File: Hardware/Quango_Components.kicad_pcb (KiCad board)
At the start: 2 copper layers, 80.7 x 100 mm, 156 parts, among them J1 Conn_01x12_Male, J2 Conn_01x12_Male, J3 Conn_01x12_Male, J4 Conn_01x12_Male, J5 SWD_Header, J6 Eurorack_10_pin_power, Q1 MMBT3904, U1 LM1117-3.3, U10 TL074, U11 TL074, U12 TL074, U13 TL074, U14 TL074, U2 STM32G473V, U3 LM1117-5.0, U4 PS508, U5 MCP6002, U6 AS3364, U7 AS3364, U8 AD5676, U9 MCP48CMB21, Y1 8MHz 20pF

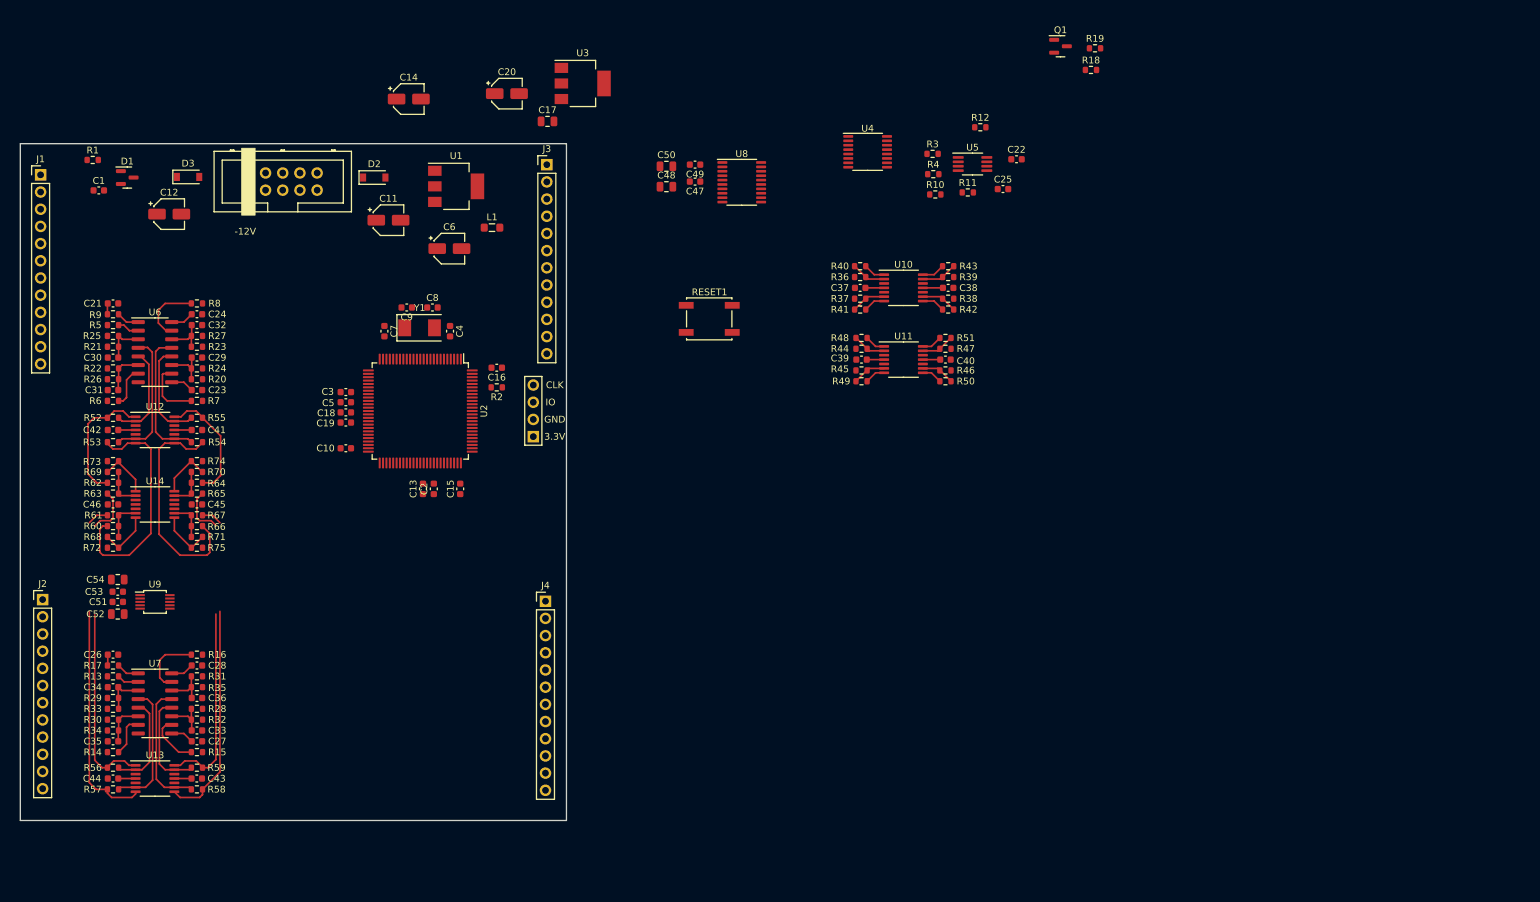
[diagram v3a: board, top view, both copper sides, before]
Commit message: Main components positioned
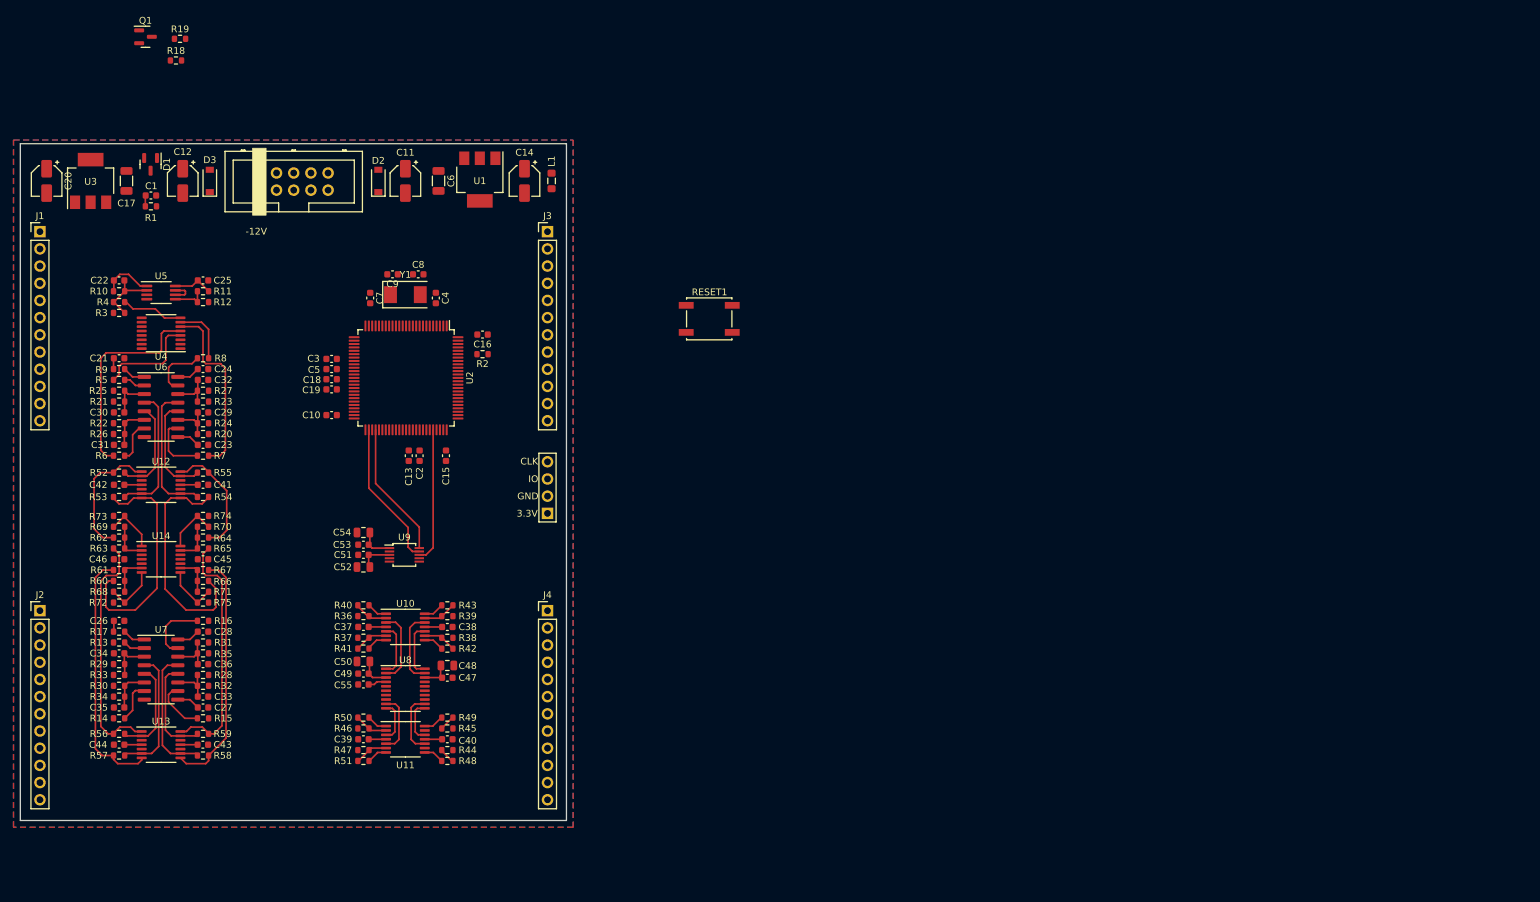
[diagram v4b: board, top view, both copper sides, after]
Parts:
- added C55: 100nF, Capacitor_SMD:C_0603_1608Metric, F.Cu at (100.8, 118.9)
- C11: value 22uF -> 47uF
- C17: footprint Capacitor_SMD:C_0805_2012Metric -> Capacitor_SMD:C_1206_3216Metric
- C6: value 22uF -> 10uF; footprint Capacitor_SMD:CP_Elec_4x5.8 -> Capacitor_SMD:C_1206_3216Metric
- moved Q1 135.2 mm to (68.6, 23.2)
- moved R18 135.2 mm to (73.1, 26.7)
- moved R19 135.2 mm to (73.7, 23.5)
- moved C22 133.8 mm to (64.7, 59.2)
- moved R3 122.5 mm to (64.7, 64.0), turned to 180 degrees
- moved R4 121.8 mm to (64.7, 62.4)
- moved R10 121.4 mm to (64.7, 60.8)
- moved U5 121.4 mm to (70.9, 61.0)
- moved C25 119.0 mm to (77.1, 59.2)
- moved R12 117.7 mm to (77.1, 62.4), turned to 180 degrees
- moved R11 113.9 mm to (77.1, 60.8)
- moved U4 107.8 mm to (70.9, 67.0), turned to 180 degrees
- moved R51 106.3 mm to (100.8, 130.2), turned to 180 degrees
- moved R47 104.5 mm to (100.8, 128.6), turned to 0 degrees
- moved R46 101.0 mm to (100.8, 125.4), turned to 0 degrees
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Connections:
- U11 pad 1: /CV_OUT_B1 -> /CV_OUT_B3
- U11 pad 10: /DAC_B3 -> /DAC_B1
- U11 pad 12: /DAC_B4 -> /DAC_B2
- U11 pad 13: Net-(R47-Pad2) -> Net-(R45-Pad2)
- U11 pad 14: /CV_OUT_B4 -> /CV_OUT_B2
- U11 pad 2: Net-(R44-Pad2) -> Net-(R46-Pad2)
- U11 pad 3: /DAC_B1 -> /DAC_B3
- U11 pad 5: /DAC_B2 -> /DAC_B4
- U11 pad 6: Net-(R45-Pad2) -> Net-(R47-Pad2)
- U11 pad 7: /CV_OUT_B2 -> /CV_OUT_B4
- U11 pad 8: /CV_OUT_B3 -> /CV_OUT_B1
- U11 pad 9: Net-(R46-Pad2) -> Net-(R44-Pad2)
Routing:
- net /AudioA2_In: track 0.00 -> 30.7 mm
- net /AudioA3_In: track 0.00 -> 26.7 mm
- net /SPI2_SCK: track 0.00 -> 21.6 mm
- net /SPI2_MOSI: track 0.00 -> 20.1 mm
- net /SPI2_MISO: track 0.00 -> 19.9 mm
- net /AudioA1_In: track 0.00 -> 15.2 mm
- net +3.3V: track 0.00 -> 13.8 mm
- net /DAC_A1: track 0.00 -> 11.1 mm
- net /DAC_A4: track 0.00 -> 11.0 mm
- net Net-(C22-Pad2): track 0.00 -> 9.47 mm
- net Net-(R4-Pad2): track 0.00 -> 9.22 mm
- net /DAC_B1: track 0.00 -> 9.10 mm
- net /DAC_B4: track 0.00 -> 9.10 mm
- net +5V: track 0.00 -> 8.97 mm
- net /AudioA4_In: track 0.00 -> 8.87 mm
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- added copper zone on B.Cu, net GND
- added copper zone on F.Cu, net GND

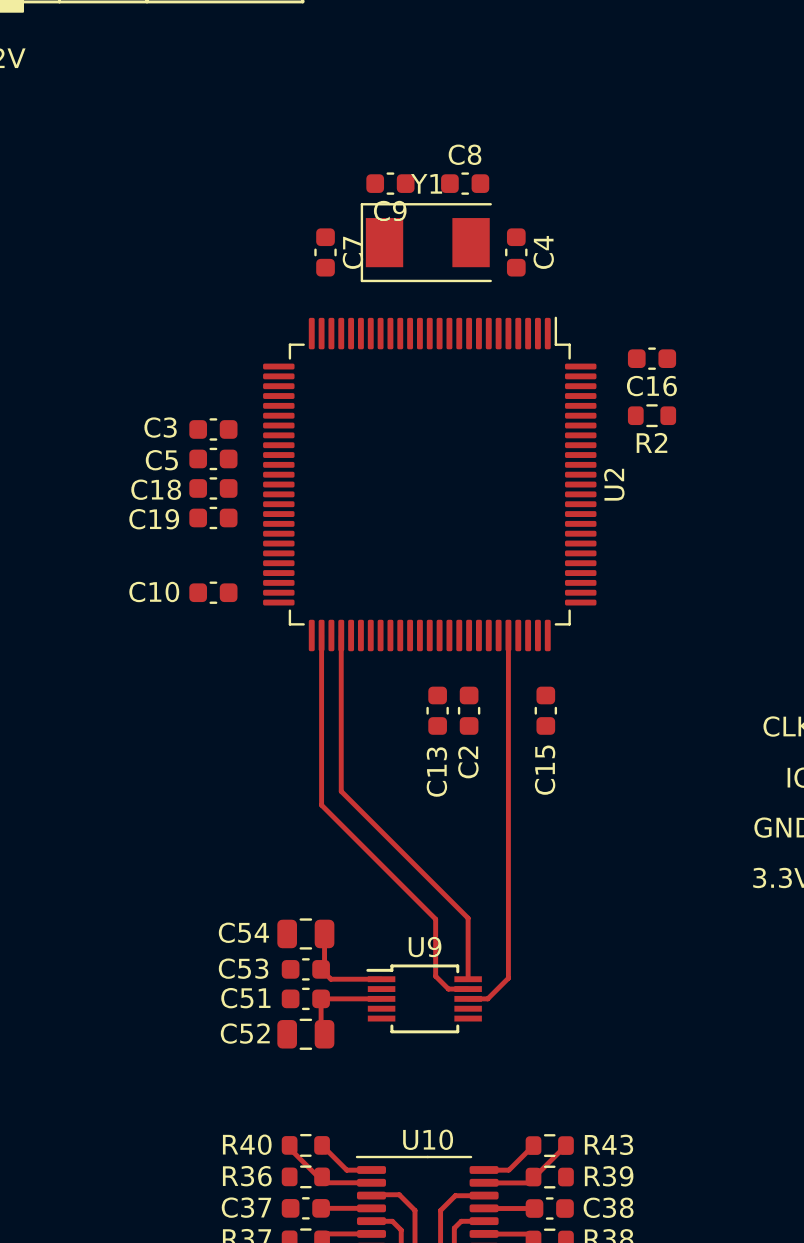
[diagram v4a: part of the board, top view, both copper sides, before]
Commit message: Added LED resistors
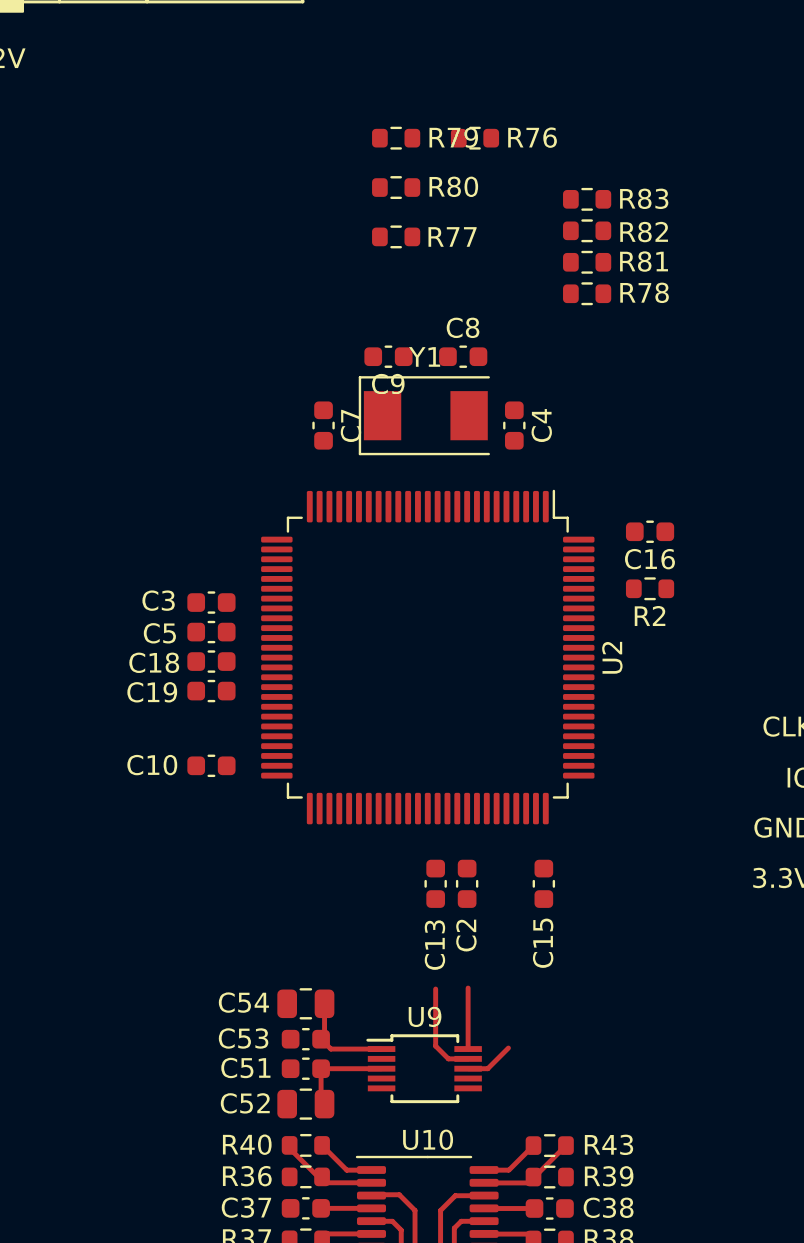
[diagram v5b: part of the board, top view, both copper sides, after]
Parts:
- added R76: 560, Resistor_SMD:R_0603_1608Metric, F.Cu at (109.4, 56.0)
- added R77: 560, Resistor_SMD:R_0603_1608Metric, F.Cu at (105.4, 61.0)
- added R78: 560, Resistor_SMD:R_0603_1608Metric, F.Cu at (115.1, 63.9)
- added R79: 560, Resistor_SMD:R_0603_1608Metric, F.Cu at (105.4, 56.0)
- added R80: 560, Resistor_SMD:R_0603_1608Metric, F.Cu at (105.4, 58.5)
- added R81: 560, Resistor_SMD:R_0603_1608Metric, F.Cu at (115.1, 62.3)
- added R82: 560, Resistor_SMD:R_0603_1608Metric, F.Cu at (115.1, 60.7)
- added R83: 560, Resistor_SMD:R_0603_1608Metric, F.Cu at (115.1, 59.1)
- moved C10 8.80 mm to (96.0, 87.9)
- moved C13 8.80 mm to (107.4, 93.9)
- moved C15 8.80 mm to (112.9, 93.9)
- moved C2 8.80 mm to (109.0, 93.9)
- moved R2 8.80 mm to (118.3, 78.9)
- moved U2 8.80 mm to (107.0, 82.4)
- moved C16 8.80 mm to (118.3, 76.0)
- moved C18 8.80 mm to (96.0, 82.6)
- moved C19 8.80 mm to (96.0, 84.1)
- moved C3 8.80 mm to (96.0, 79.6)
- moved C4 8.80 mm to (111.4, 70.6)
- moved C5 8.80 mm to (96.0, 81.1)
- moved C7 8.80 mm to (101.7, 70.6)
- moved C8 8.80 mm to (108.8, 67.1)
- moved C9 8.80 mm to (105.0, 67.1)
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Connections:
- J1 pad 1: /EnvA1_LED -> /EnvA1_LED_Out
- J1 pad 2: /EnvA2_LED -> /EnvA2_LED_Out
- J1 pad 3: /EnvA3_LED -> /EnvA3_LED_Out
- J1 pad 4: /EnvA4_LED -> /EnvA4_LED_Out
- J1 pad 5: /EnvB1_LED -> /EnvB1_LED_Out
- J1 pad 6: /EnvB2_LED -> /EnvB2_LED_Out
- J1 pad 7: /EnvB3_LED -> /EnvB3_LED_Out
- J1 pad 8: /EnvB4_LED -> /EnvB4_LED_Out
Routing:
- net /SPI2_MISO: track 19.9 -> 2.48 mm
- net /SPI2_MOSI: track 20.1 -> 3.10 mm
- net /SPI2_SCK: track 21.6 -> 4.82 mm

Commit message: More Layout
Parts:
- added R84: 560, Resistor_SMD:R_0603_1608Metric, F.Cu at (113.2, 119.9)
- added R85: 560, Resistor_SMD:R_0603_1608Metric, F.Cu at (113.2, 104.3)
- J1, J2, J3, J4: moved to B.Cu
- moved RESET1 45.7 mm to (106.8, 57.5)
- moved R79 13.2 mm to (118.1, 59.5), turned to 180 degrees
- moved R80 12.7 mm to (118.1, 57.9), turned to 180 degrees
- moved R77 12.7 mm to (118.1, 61.1), turned to 180 degrees
- moved R76 11.0 mm to (118.1, 62.7), turned to 180 degrees
- moved R81 6.71 mm to (118.1, 56.3), turned to 180 degrees
- moved R82 6.71 mm to (118.1, 54.7), turned to 180 degrees
- moved R83 6.71 mm to (118.1, 53.1), turned to 180 degrees
- moved R78 3.03 mm to (118.1, 64.3), turned to 180 degrees
- moved C15 0.10 mm to (113.0, 93.9)
- turned J1 to 180 degrees
- turned J2 to 180 degrees
- turned J3 to 180 degrees
- turned J4 to 180 degrees
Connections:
- J1 pad 1: /EnvA1_LED_Out -> /Env1_Attack
- J1 pad 2: /EnvA2_LED_Out -> /Env1_Decay
- J1 pad 3: /EnvA3_LED_Out -> /Env1_Sustain
- J1 pad 4: /EnvA4_LED_Out -> /Env1_Release
- J1 pad 5: /EnvB1_LED_Out -> /Env2_Attack
- J1 pad 6: /EnvB2_LED_Out -> /Env2_Decay
- J1 pad 7: /EnvB3_LED_Out -> /Env2_Sustain
- J1 pad 8: /EnvB4_LED_Out -> /Env2_Release
- J3 pad 1: /CV_OUT_A1 -> /EnvA1_LED_Out
- J3 pad 2: /CV_OUT_A2 -> /EnvA2_LED_Out
- J3 pad 3: /CV_OUT_A3 -> /EnvA3_LED_Out
- J3 pad 4: /CV_OUT_A4 -> /EnvA4_LED_Out
- J3 pad 5: /CV_OUT_B1 -> /EnvB1_LED_Out
- J3 pad 6: /CV_OUT_B2 -> /EnvB2_LED_Out
- J3 pad 7: /CV_OUT_B3 -> /EnvB3_LED_Out
- J3 pad 8: /CV_OUT_B4 -> /EnvB4_LED_Out
- J4 pad 1: /Env1_Attack -> +3.3VA
- J4 pad 10: /Calib_Btn1 -> /CV_OUT_B1
- J4 pad 11: /Calib_Btn2 -> /CV_OUT_B4
- J4 pad 12: GND -> /CV_OUT_B3
- J4 pad 2: /Env1_Decay -> /Calib_Btn1
- J4 pad 3: /Env1_Sustain -> /Calib_Btn2
- J4 pad 4: /Env1_Release -> GND
- J4 pad 5: /Env2_Attack -> /CV_OUT_A2
- J4 pad 6: /Env2_Decay -> /CV_OUT_A1
- J4 pad 7: /Env2_Sustain -> /CV_OUT_A4
- J4 pad 8: /Env2_Release -> /CV_OUT_A3
- J4 pad 9: +3.3VA -> /CV_OUT_B2
- U8 pad 15: GND -> Net-(U8-Pad15)
- U9 pad 6: GND -> Net-(U9-Pad6)
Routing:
- net /CV_OUT_A2: track 3.05 -> 50.3 mm
- net /CV_OUT_B3: track 3.03 -> 47.6 mm
- net /CV_OUT_A1: track 3.31 -> 35.7 mm
- net /CV_OUT_B4: track 3.01 -> 30.7 mm
- net /EnvB4_LED: track 0.00 -> 25.9 mm
- net /CV_OUT_A4: track 3.03 -> 28.0 mm
- net /EnvB3_LED: track 0.00 -> 23.7 mm
- net /EnvA4_LED: track 0.00 -> 22.8 mm
- net /EnvB2_LED: track 0.00 -> 21.6 mm
- net /CV_OUT_A3: track 3.03 -> 23.7 mm
- net /EnvB1_LED: track 0.00 -> 19.5 mm
- net /CV_OUT_B2: track 2.96 -> 21.4 mm
- net +3.3V: track 13.8 -> 31.7 mm
- net /CV_OUT_B1: track 3.03 -> 19.1 mm
- net /SWCLK: track 0.00 -> 14.1 mm
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
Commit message: Further Layout
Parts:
- turned RESET1 to 180 degrees
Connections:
- J1 pad 1: /Env1_Attack -> /AudioA1_In
- J1 pad 10: /Audio2_Out -> /Env2_Decay
- J1 pad 11: /Audio3_Out -> /Env2_Sustain
- J1 pad 12: /Audio4_Out -> /Env2_Release
- J1 pad 2: /Env1_Decay -> /AudioA2_In
- J1 pad 3: /Env1_Sustain -> /AudioA3_In
- J1 pad 4: /Env1_Release -> /AudioA4_In
- J1 pad 5: /Env2_Attack -> /Env1_Attack
- J1 pad 6: /Env2_Decay -> /Env1_Decay
- J1 pad 7: /Env2_Sustain -> /Env1_Sustain
- J1 pad 8: /Env2_Release -> /Env1_Release
- J1 pad 9: /Audio1_Out -> /Env2_Attack
- J2 pad 1: /AudioA1_In -> /Audio2_Out
- J2 pad 2: /AudioA2_In -> /Audio3_Out
- J2 pad 3: /AudioA3_In -> /Audio4_Out
- J2 pad 4: /AudioA4_In -> /Audio1_Out
- J3 pad 1: /EnvA1_LED_Out -> /EnvB4_LED_Out
- J3 pad 2: /EnvA2_LED_Out -> /EnvB3_LED_Out
- J3 pad 3: /EnvA3_LED_Out -> /EnvB2_LED_Out
- J3 pad 4: /EnvA4_LED_Out -> /EnvB1_LED_Out
- J3 pad 5: /EnvB1_LED_Out -> /EnvA4_LED_Out
- J3 pad 6: /EnvB2_LED_Out -> /EnvA2_LED_Out
- J3 pad 7: /EnvB3_LED_Out -> /EnvA1_LED_Out
- J3 pad 8: /EnvB4_LED_Out -> /EnvA3_LED_Out
- U2 pad 22: /EnvA1_DAC -> /EnvA2_DAC
- U2 pad 26: /EnvA2_DAC -> /EnvA1_DAC
- U2 pad 27: /EnvA3_DAC -> /EnvA4_DAC
- U2 pad 28: /EnvA4_DAC -> /EnvA3_DAC
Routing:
- net +12V: track 17.9 -> 83.9 mm
- net /Env1_Attack: track 0.00 -> 62.6 mm, vias 0 -> 1
- net /Env1_Decay: track 0.00 -> 61.6 mm, vias 0 -> 1
- net /Env1_Sustain: track 0.00 -> 60.8 mm, vias 0 -> 1
- net /Env1_Release: track 0.00 -> 59.9 mm, vias 0 -> 1
- net /Env2_Attack: track 0.00 -> 59.6 mm, vias 0 -> 1
- net /EnvA2_DAC: track 0.00 -> 55.3 mm
- net /Env2_Decay: track 0.00 -> 50.5 mm, vias 0 -> 1
- net /EnvA1_DAC: track 0.00 -> 50.0 mm
- net /Env2_Sustain: track 0.00 -> 49.8 mm, vias 0 -> 1
- net /Env2_Release: track 0.00 -> 49.6 mm, vias 0 -> 1
- net /EnvB3_DAC: track 0.00 -> 37.0 mm
- net /Audio3_Out: track 0.00 -> 32.7 mm, vias 0 -> 1
- net /OpAmps/AudioB4_Out: track 35.9 -> 5.47 mm
- net /Audio4_Out: track 0.00 -> 30.3 mm, vias 0 -> 1
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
